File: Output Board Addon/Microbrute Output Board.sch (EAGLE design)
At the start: 28 parts, among them U1 TL074_SMD

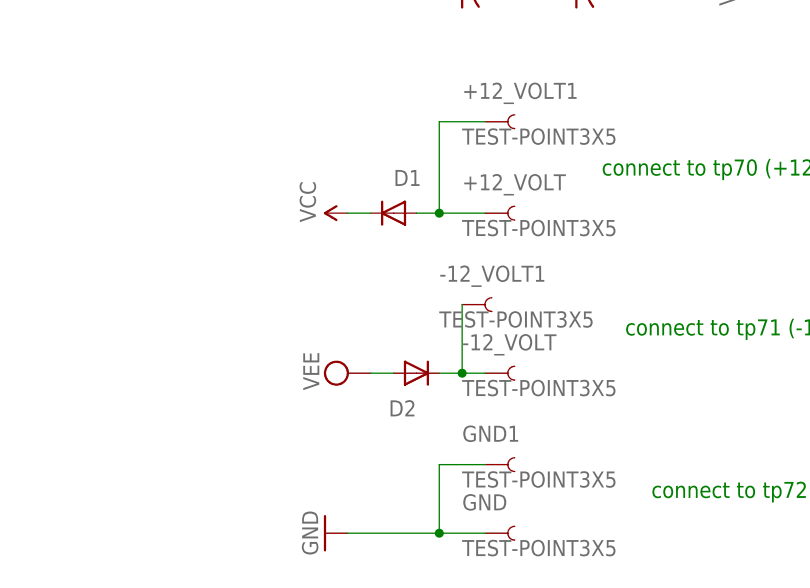
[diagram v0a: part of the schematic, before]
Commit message: Fixed vital problem: Orientation of power diodes was wrong
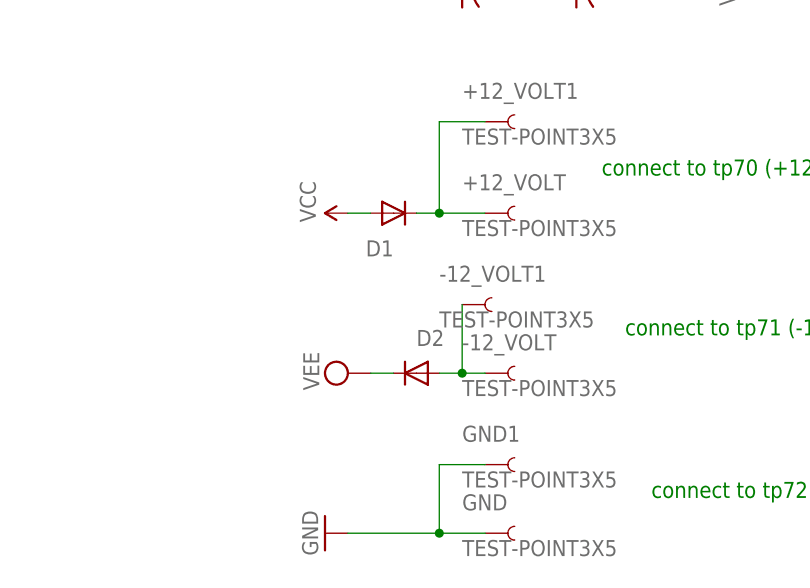
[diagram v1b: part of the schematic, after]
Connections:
- net N$1: now also D1.C; no longer D1.A
- net N$2: now also D2.A; no longer D2.C
- net VCC: now also D1.A; no longer D1.C
- net VEE: now also D2.C; no longer D2.A
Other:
- moved on the sheet: D1, D2
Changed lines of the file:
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@@
 <layer number="255" name="routoute" color="7" fill="1" visible="yes" active="yes"/>
 </layers>
-<schematic xreflabel="%F%N/%S.%C%R" xrefpart="/%S.%C%R">
+<schematic xreflabel="%F%N/%S" xrefpart="/%S.%C%R">
 <attributes>
 </attributes>
@@
 <instance part="FRAME1" gate="G$1" x="0" y="0"/>
 <instance part="FRAME1" gate="V" x="147.32" y="0"/>
-<instance part="D1" gate="G$1" x="182.88" y="99.06" smashed="yes" rot="R180">
-<attribute name="NAME" x="182.88" y="102.0826" size="1.778" layer="95"/>
+<instance part="D1" gate="G$1" x="182.88" y="99.06" smashed="yes">
+<attribute name="NAME" x="182.88" y="96.0374" size="1.778" layer="95" rot="R180"/>
 </instance>
-<instance part="D2" gate="G$1" x="185.42" y="81.28" smashed="yes">
-<attribute name="NAME" x="185.42" y="78.2574" size="1.778" layer="95" rot="R180"/>
+<instance part="D2" gate="G$1" x="185.42" y="81.28" smashed="yes" rot="R180">
+<attribute name="NAME" x="185.42" y="84.3026" size="1.778" layer="95"/>
 </instance>
 <instance part="OUT2" gate="G$1" x="101.6" y="71.12"/>
@@
 <net name="VEE" class="0">
 <segment>
-<pinref part="D2" gate="G$1" pin="A"/>
-<pinref part="SUPPLY4" gate="G$1" pin="VEE"/>
-<wire x1="182.88" y1="81.28" x2="180.34" y2="81.28" width="0.1524" layer="91"/>
-</segment>
-<segment>
 <wire x1="208.28" y1="124.46" x2="210.82" y2="124.46" width="0.1524" layer="91"/>
 <wire x1="210.82" y1="124.46" x2="210.82" y2="132.08" width="0.1524" layer="91"/>
@@
 <wire x1="205.74" y1="132.08" x2="210.82" y2="132.08" width="0.1524" layer="91"/>
 </segment>
+<segment>
+<pinref part="D2" gate="G$1" pin="C"/>
+<pinref part="SUPPLY4" gate="G$1" pin="VEE"/>
+<wire x1="182.88" y1="81.28" x2="180.34" y2="81.28" width="0.1524" layer="91"/>
+</segment>
 </net>
 <net name="VCC" class="0">
-<segment>
-<pinref part="D1" gate="G$1" pin="C"/>
-<pinref part="P+4" gate="1" pin="VCC"/>
-<wire x1="180.34" y1="99.06" x2="177.8" y2="99.06" width="0.1524" layer="91"/>
-</segment>
 <segment>
 <wire x1="185.42" y1="124.46" x2="187.96" y2="124.46" width="0.1524" layer="91"/>
@@
 <wire x1="190.5" y1="132.08" x2="185.42" y2="132.08" width="0.1524" layer="91"/>
 </segment>
+<segment>
+<pinref part="D1" gate="G$1" pin="A"/>
+<pinref part="P+4" gate="1" pin="VCC"/>
+<wire x1="180.34" y1="99.06" x2="177.8" y2="99.06" width="0.1524" layer="91"/>
+</segment>
 </net>
 <net name="N$1" class="0">
 <segment>
-<pinref part="D1" gate="G$1" pin="A"/>
 <pinref part="+12_VOLT" gate="G$1" pin="1"/>
-<wire x1="185.42" y1="99.06" x2="187.96" y2="99.06" width="0.1524" layer="91"/>
 <pinref part="+12_VOLT1" gate="G$1" pin="1"/>
 <wire x1="187.96" y1="99.06" x2="193.04" y2="99.06" width="0.1524" layer="91"/>
 <wire x1="193.04" y1="109.22" x2="187.96" y2="109.22" width="0.1524" layer="91"/>
 <wire x1="187.96" y1="109.22" x2="187.96" y2="99.06" width="0.1524" layer="91"/>
+<pinref part="D1" gate="G$1" pin="C"/>
+<wire x1="185.42" y1="99.06" x2="187.96" y2="99.06" width="0.1524" layer="91"/>
 <junction x="187.96" y="99.06"/>
 </segment>
@@
 <net name="N$2" class="0">
 <segment>
-<pinref part="D2" gate="G$1" pin="C"/>
 <pinref part="-12_VOLT" gate="G$1" pin="1"/>
-<wire x1="187.96" y1="81.28" x2="190.5" y2="81.28" width="0.1524" layer="91"/>
 <pinref part="-12_VOLT1" gate="G$1" pin="1"/>
 <wire x1="190.5" y1="81.28" x2="193.04" y2="81.28" width="0.1524" layer="91"/>
 <wire x1="190.5" y1="88.9" x2="190.5" y2="81.28" width="0.1524" layer="91"/>
+<pinref part="D2" gate="G$1" pin="A"/>
+<wire x1="187.96" y1="81.28" x2="190.5" y2="81.28" width="0.1524" layer="91"/>
 <junction x="190.5" y="81.28"/>
 </segment>
